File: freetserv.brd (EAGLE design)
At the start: 91.4 x 82.5 mm, 157 parts, among them IC1 MCP16311-E/MS, IC10 MAX3232ECPW, IC11 MAX3232ECPW, IC12 MAX3232ECPW, IC13 MAX3232ECPW, IC14 FT4232HL, IC15 MAX3232ECPW, IC16 MAX3232ECPW, IC17 MAX3232ECPW, IC18 MAX3232ECPW, IC3 TUSB2046BVF, IC4 FT4232HL, IC5 MAX3232ECPW, IC6 MAX3232ECPW, IC7 MAX3232ECPW, IC8 MAX3232ECPW, IC9 FT4232HL, Q2 6MHz

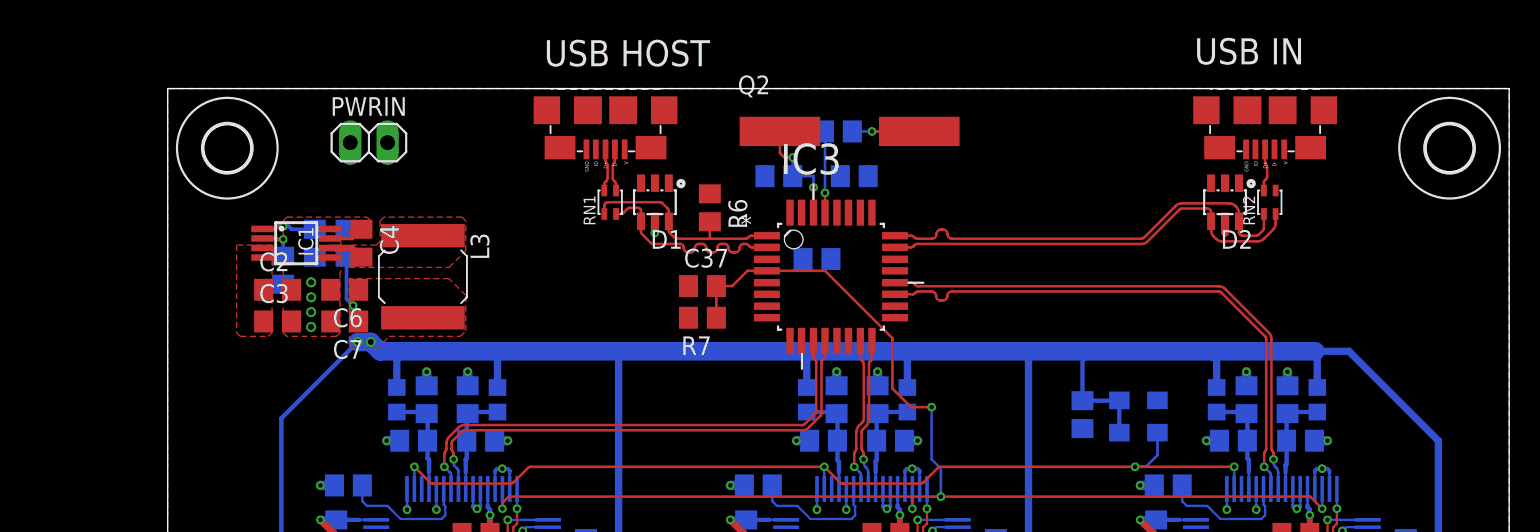
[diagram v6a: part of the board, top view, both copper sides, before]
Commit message: add daisy-chain input/output socket/pin headers
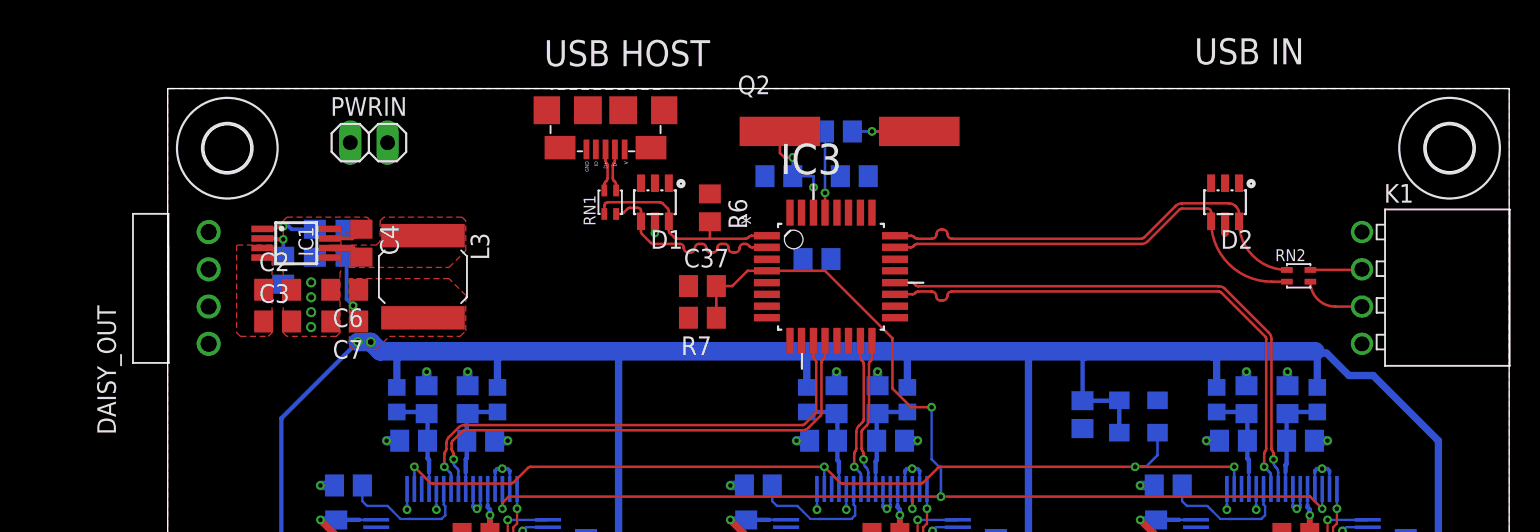
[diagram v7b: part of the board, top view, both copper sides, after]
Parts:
- removed USB_OUT: USB_MICROB, ftdi_ft231xq-r:USB_MICROB_PACKAGE
- added DAISY_OUT: 61300411021, Wurth_Elektronik_Electromechanic_Board_to_Board_Connectors_rev15c:61300411021
- added K1: 613004143121, Wurth_Elektronik_Electromechanic_Board_to_Board_Connectors_rev15c:613004143121
- moved RN2 5.39 mm to (77.1, 69.8), turned to 270 degrees
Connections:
- removed net DX1_P: RN2.A2, USB_OUT.D+
- new net N$15: K1.4
- new net N$8: K1.3, RN2.B2
- net +5V: now also DAISY_OUT.1, K1.1
- net DX0_N: now also DAISY_OUT.3
- net DX0_P: now also DAISY_OUT.2
- net GND: now also DAISY_OUT.4; no longer USB_OUT.GND
- net N$7: now also K1.2, RN2.A2; no longer RN2.B2, USB_OUT.D-
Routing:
- net N$8: track 0.00 -> 4.22 mm
- net N$7: track 0.00 -> 3.56 mm
- net DX1_P: track 2.89 -> 0.00 mm
- net D1_P: track 29.6 -> 30.5 mm

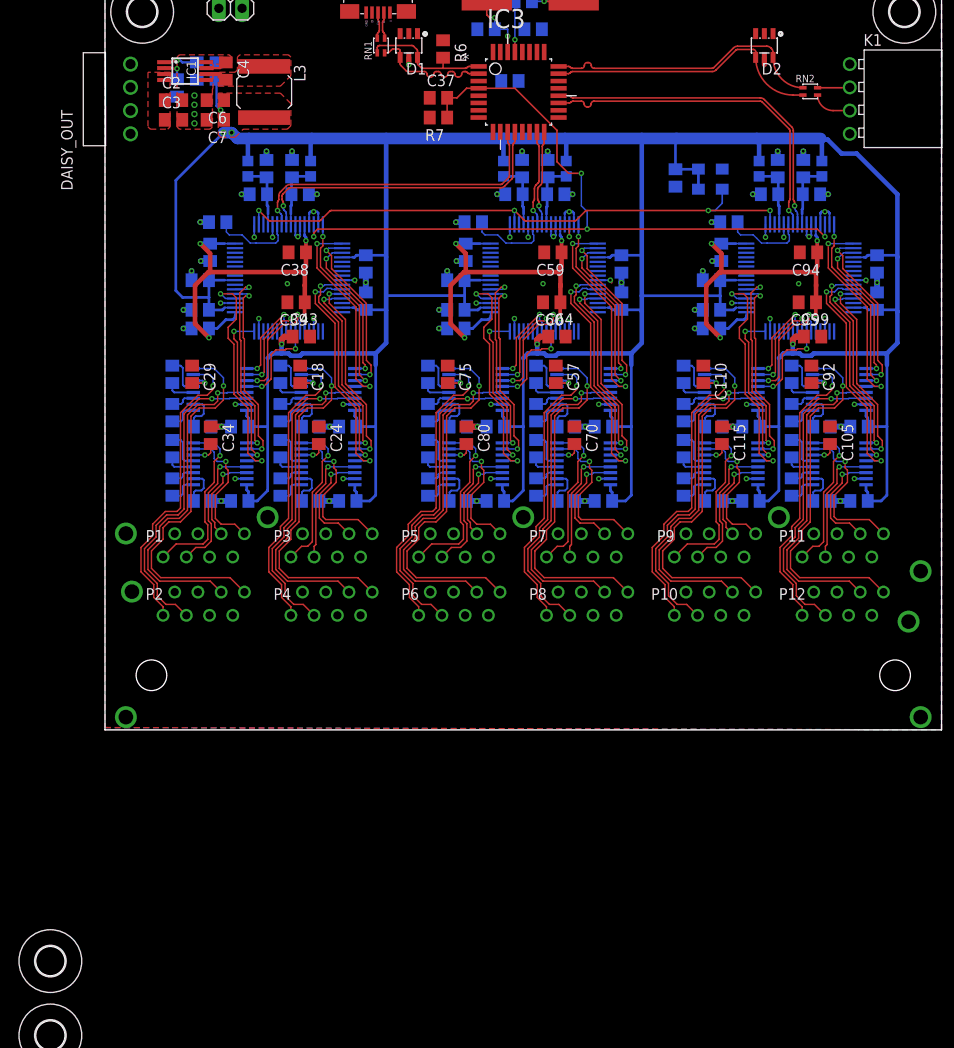
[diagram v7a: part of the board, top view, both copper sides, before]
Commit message: drc: fix via size, width on bottom layer
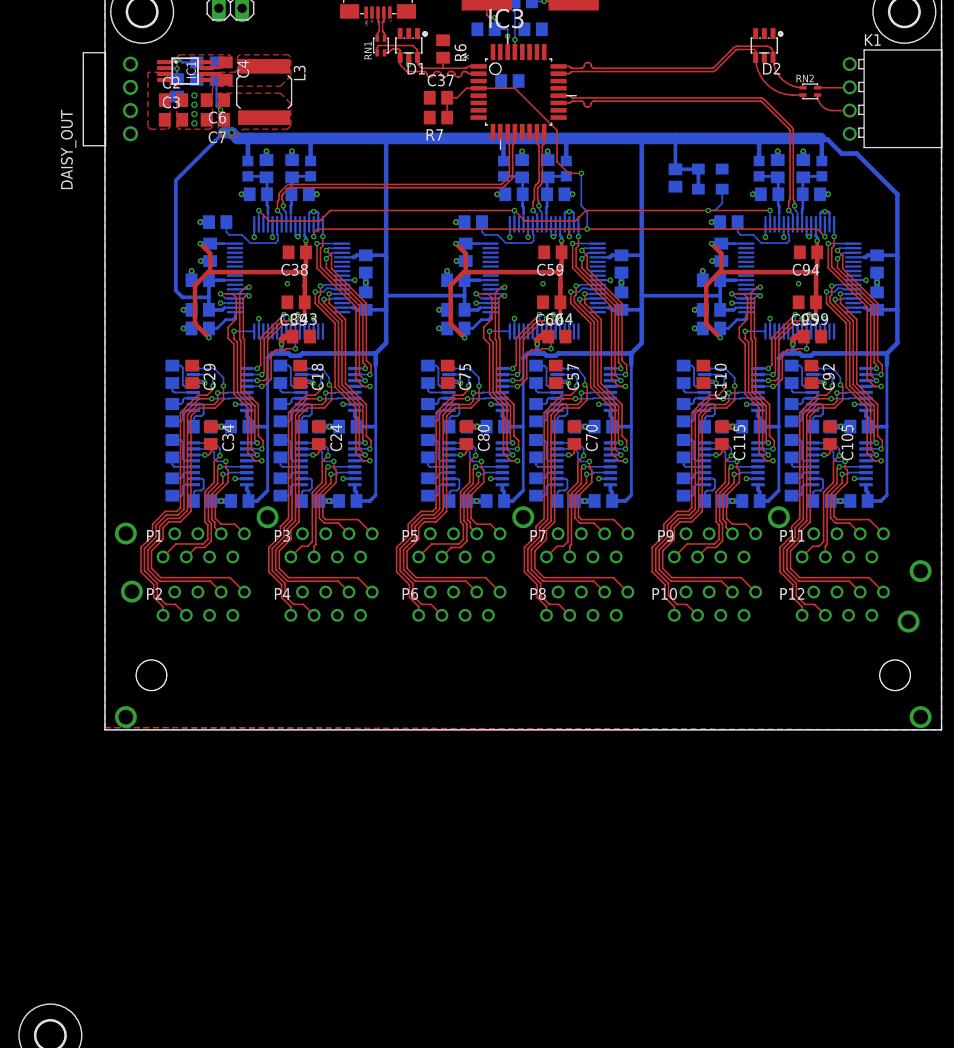
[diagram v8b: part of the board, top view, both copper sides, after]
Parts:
- removed H3: MOUNT-HOLE3.2, holes:3,2
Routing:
- net GND1: track 0.80 -> 0.00 mm
